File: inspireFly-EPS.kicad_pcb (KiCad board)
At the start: 4 copper layers, 88 x 94.5 mm, 2 parts

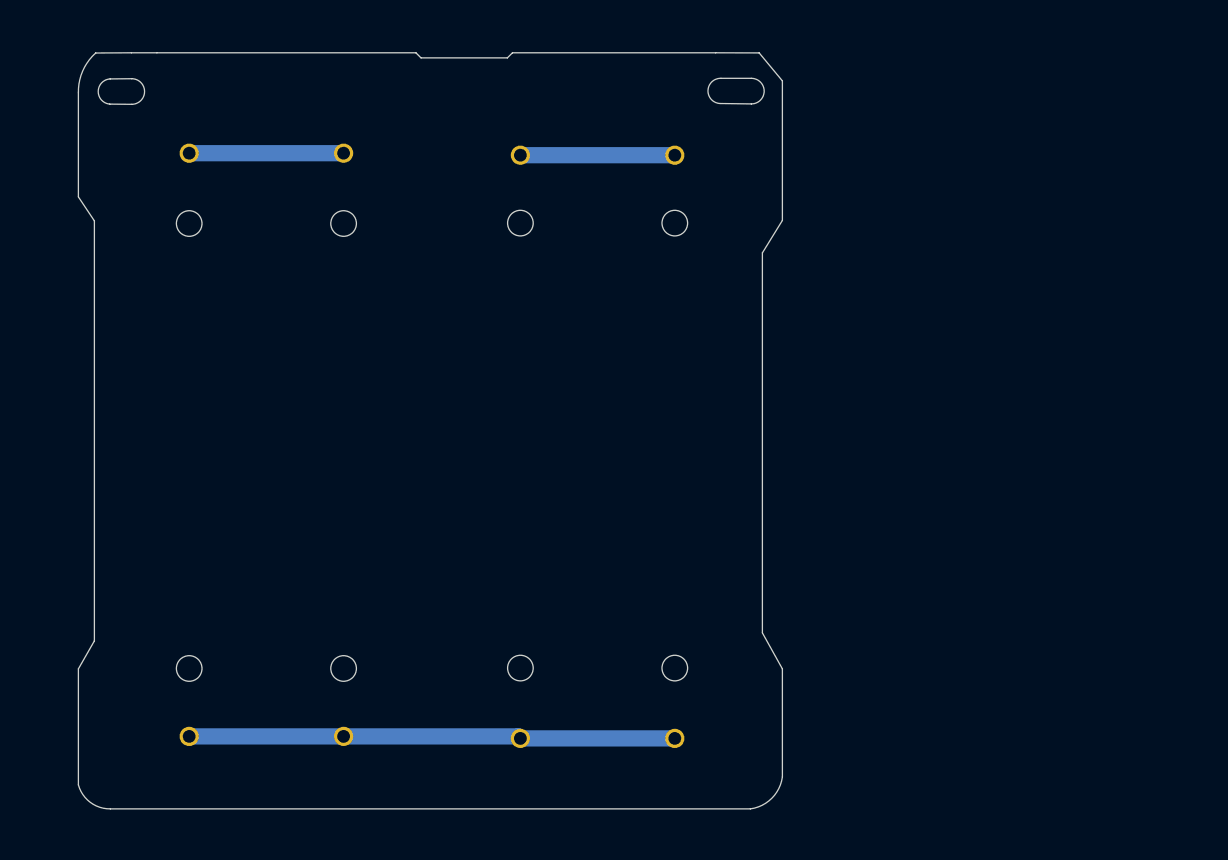
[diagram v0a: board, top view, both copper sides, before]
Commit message: Updates to BQ chip and routing
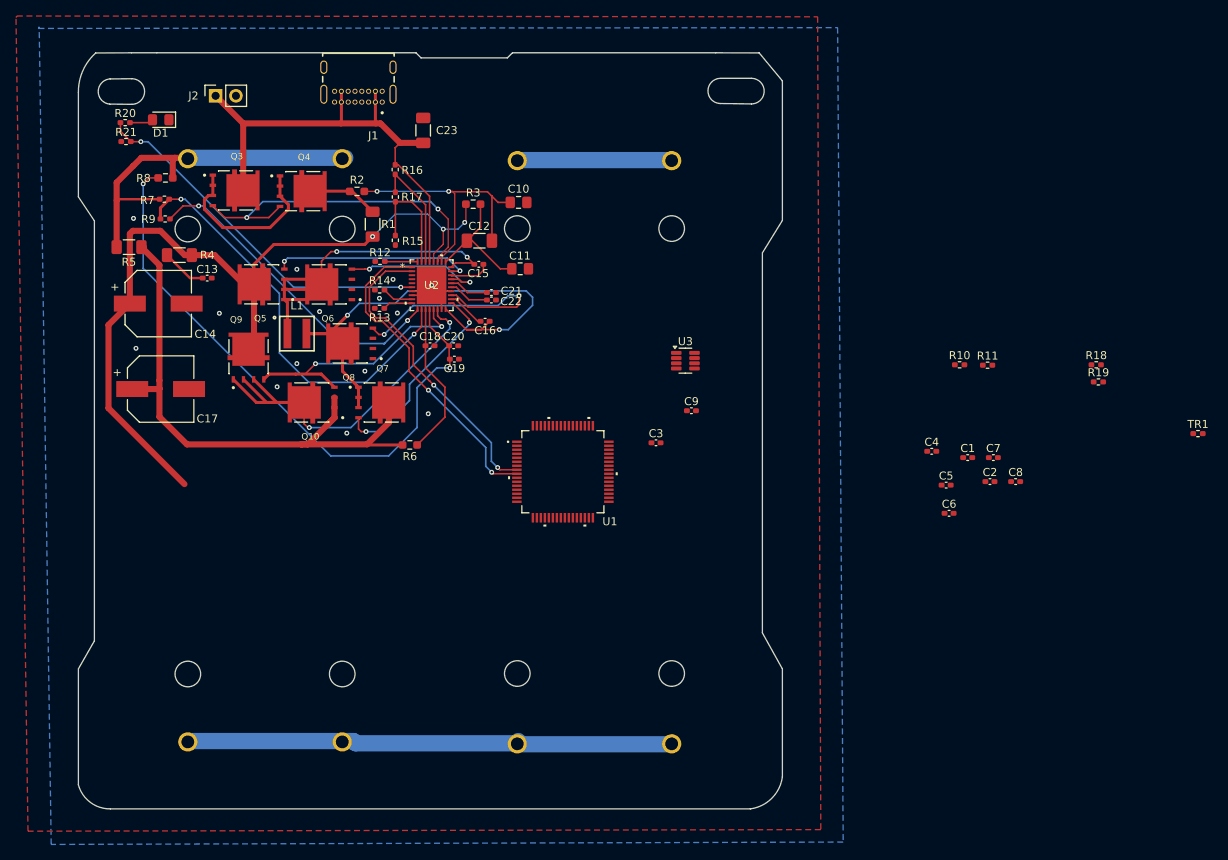
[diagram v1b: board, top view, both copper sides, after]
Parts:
- removed REF** (x2): BAT_BK-18650-PC4, inspireFly-EPS-footprints:BAT_BK-18650-PC4
- added BT1: BK-18650-PC4, inspireFly-EPS-footprints:BAT_BK-18650-PC4, B.Cu at (61.3, 74.8)
- added BT2: BK-18650-PC4, inspireFly-EPS-footprints:BAT_BK-18650-PC4, B.Cu at (102.5, 74.8)
- added C1: 100nF, Capacitor_SMD:C_0402_1005Metric_Pad0.74x0.62mm_HandSolder, F.Cu at (149.2, 75.6)
- added C10: 100nF, Capacitor_SMD:C_0805_2012Metric_Pad1.18x1.45mm_HandSolder, F.Cu at (93.0, 43.7)
- added C11: 100nF, Capacitor_SMD:C_0805_2012Metric_Pad1.18x1.45mm_HandSolder, F.Cu at (93.2, 52.0)
- added C12: 470nF, Capacitor_SMD:C_1206_3216Metric_Pad1.33x1.80mm_HandSolder, F.Cu at (88.1, 48.5)
- added C13: 2.2uF, Capacitor_SMD:C_0402_1005Metric_Pad0.74x0.62mm_HandSolder, F.Cu at (54.1, 53.2)
- added C14: 47uF, inspireFly-EPS-footprints:CAP_EEEFN1J470L, F.Cu at (48.0, 56.4)
- added C15: 47nF, Capacitor_SMD:C_0402_1005Metric_Pad0.74x0.62mm_HandSolder, F.Cu at (88.1, 51.4)
- added C16: 47nF, Capacitor_SMD:C_0402_1005Metric_Pad0.74x0.62mm_HandSolder, F.Cu at (88.8, 58.6)
- added C17: 47uF, inspireFly-EPS-footprints:CAP_EEEFN1J470L, F.Cu at (48.3, 67.0)
- added C18: 100nF, Capacitor_SMD:C_0402_1005Metric_Pad0.74x0.62mm_HandSolder, F.Cu at (82.0, 61.6)
- added C19: 100nF, Capacitor_SMD:C_0402_1005Metric_Pad0.74x0.62mm_HandSolder, F.Cu at (85.0, 63.3)
- added C2: 4.7uF, Capacitor_SMD:C_0402_1005Metric_Pad0.74x0.62mm_HandSolder, F.Cu at (151.9, 78.6)
- added C20: 470nF, Capacitor_SMD:C_0402_1005Metric_Pad0.74x0.62mm_HandSolder, F.Cu at (84.9, 61.6)
- added C21: 4.7uF, Capacitor_SMD:C_0402_1005Metric_Pad0.74x0.62mm_HandSolder, F.Cu at (89.6, 55.0)
- added C22: 4.7uF, Capacitor_SMD:C_0402_1005Metric_Pad0.74x0.62mm_HandSolder, F.Cu at (89.6, 55.9)
- added C23: 2.2uF, Capacitor_SMD:C_1206_3216Metric_Pad1.33x1.80mm_HandSolder, F.Cu at (81.1, 34.7)
- added C3: 100nF, Capacitor_SMD:C_0402_1005Metric_Pad0.74x0.62mm_HandSolder, F.Cu at (110.2, 73.8)
- added C4: 100nF, Capacitor_SMD:C_0402_1005Metric_Pad0.74x0.62mm_HandSolder, F.Cu at (144.7, 74.8)
- added C5: 100nF, Capacitor_SMD:C_0402_1005Metric_Pad0.74x0.62mm_HandSolder, F.Cu at (146.5, 79.0)
- added C6: 10uF, Capacitor_SMD:C_0402_1005Metric_Pad0.74x0.62mm_HandSolder, F.Cu at (146.8, 82.6)
- added C7: 1uF, Capacitor_SMD:C_0402_1005Metric_Pad0.74x0.62mm_HandSolder, F.Cu at (152.4, 75.6)
- added C8: 100nF, Capacitor_SMD:C_0402_1005Metric_Pad0.74x0.62mm_HandSolder, F.Cu at (155.2, 78.6)
- added C9: 100nF, Capacitor_SMD:C_0402_1005Metric_Pad0.74x0.62mm_HandSolder, F.Cu at (114.6, 69.7)
- added D1: LED, Diode_SMD:D_0805_2012Metric_Pad1.15x1.40mm_HandSolder, F.Cu at (48.3, 33.4)
- added J1: USB4085-GF-A_REVB, inspireFly-EPS-footprints:GCT_USB4085-GF-A_REVB, F.Cu at (73.0, 26.8)
- added J2: Conn_01x02_Pin, Connector_PinSocket_2.54mm:PinSocket_1x02_P2.54mm_Vertical, F.Cu at (55.1, 30.4)
- added L1: 2.2uH, inspireFly-EPS-footprints:WE-MXGI_4020, F.Cu at (65.3, 60.1)
- added Q10: SQJA62EP-T1_GE3, inspireFly-EPS-footprints:TRANS_SQJA62EP-T1_GE3, F.Cu at (67.3, 68.7)
- added Q3: SQJA62EP-T1_GE3, inspireFly-EPS-footprints:TRANS_SQJA62EP-T1_GE3, F.Cu at (57.5, 42.2)
- added Q4: SQJA62EP-T1_GE3, inspireFly-EPS-footprints:TRANS_SQJA62EP-T1_GE3, F.Cu at (65.9, 42.3)
- added Q5: SQJA62EP-T1_GE3, inspireFly-EPS-footprints:TRANS_SQJA62EP-T1_GE3, F.Cu at (61.0, 53.9)
- added Q6: SQJA62EP-T1_GE3, inspireFly-EPS-footprints:TRANS_SQJA62EP-T1_GE3, F.Cu at (69.5, 54.0)
- added Q7: SQJA62EP-T1_GE3, inspireFly-EPS-footprints:TRANS_SQJA62EP-T1_GE3, F.Cu at (75.7, 68.7)
- added Q8: SQJA62EP-T1_GE3, inspireFly-EPS-footprints:TRANS_SQJA62EP-T1_GE3, F.Cu at (72.1, 61.3)
- added Q9: SQJA62EP-T1_GE3, inspireFly-EPS-footprints:TRANS_SQJA62EP-T1_GE3, F.Cu at (59.3, 63.1)
- added R1: 5m, Resistor_SMD:R_1206_3216Metric_Pad1.30x1.75mm_HandSolder, F.Cu at (74.8, 46.4)
- added R10: 5.24k, Resistor_SMD:R_0402_1005Metric_Pad0.72x0.64mm_HandSolder, F.Cu at (148.2, 64.0)
- added R11: 30.31k, Resistor_SMD:R_0402_1005Metric_Pad0.72x0.64mm_HandSolder, F.Cu at (151.7, 64.0)
- added R12: 40k, Resistor_SMD:R_0402_1005Metric_Pad0.72x0.64mm_HandSolder, F.Cu at (75.7, 51.1)
- added R13: 3.3k, Resistor_SMD:R_0402_1005Metric_Pad0.72x0.64mm_HandSolder, F.Cu at (75.6, 56.9)
- added R14: 12.5k, Resistor_SMD:R_0402_1005Metric_Pad0.72x0.64mm_HandSolder, F.Cu at (75.7, 54.6)
- added R15: 22.6k, Resistor_SMD:R_0402_1005Metric_Pad0.72x0.64mm_HandSolder, F.Cu at (77.6, 48.4)
- added R16: 1M, Resistor_SMD:R_0402_1005Metric_Pad0.72x0.64mm_HandSolder, F.Cu at (77.6, 39.6)
- added R17: 100k, Resistor_SMD:R_0402_1005Metric_Pad0.72x0.64mm_HandSolder, F.Cu at (77.6, 43.0)
- added R18: 10k, Resistor_SMD:R_0402_1005Metric_Pad0.72x0.64mm_HandSolder, F.Cu at (165.2, 64.0)
- added R19: 10k, Resistor_SMD:R_0402_1005Metric_Pad0.72x0.64mm_HandSolder, F.Cu at (165.5, 66.1)
- added R2: 10, Resistor_SMD:R_0603_1608Metric_Pad0.98x0.95mm_HandSolder, F.Cu at (72.8, 42.3)
- added R20: 330, Resistor_SMD:R_0402_1005Metric_Pad0.72x0.64mm_HandSolder, F.Cu at (43.9, 33.7)
- added R21: 10K, Resistor_SMD:R_0402_1005Metric_Pad0.72x0.64mm_HandSolder, F.Cu at (44.0, 36.1)
- added R3: 10, Resistor_SMD:R_0603_1608Metric_Pad0.98x0.95mm_HandSolder, F.Cu at (87.3, 43.9)
- added R4: 2, Resistor_SMD:R_1206_3216Metric_Pad1.30x1.75mm_HandSolder, F.Cu at (50.6, 50.3)
- added R5: 5m, Resistor_SMD:R_1206_3216Metric_Pad1.30x1.75mm_HandSolder, F.Cu at (44.3, 49.3)
- added R6: 10, Resistor_SMD:R_0603_1608Metric_Pad0.98x0.95mm_HandSolder, F.Cu at (79.4, 74.0)
- added R7: 10, Resistor_SMD:R_0603_1608Metric_Pad0.98x0.95mm_HandSolder, F.Cu at (48.9, 40.6)
- added R8: 200k, Resistor_SMD:R_0402_1005Metric_Pad0.72x0.64mm_HandSolder, F.Cu at (48.8, 43.3)
- added R9: 44.8k, Resistor_SMD:R_0402_1005Metric_Pad0.72x0.64mm_HandSolder, F.Cu at (48.9, 45.8)
- added TR1: 120, Resistor_SMD:R_0402_1005Metric_Pad0.72x0.64mm_HandSolder, F.Cu at (177.9, 72.6)
- added U1: STM32U575RIT6, inspireFly-EPS-footprints:LQFP64-10x10mm_STM, F.Cu at (98.6, 77.4)
- added U2: BQ25750RRVR, inspireFly-EPS-footprints:VQFN36_RRV_TEX, F.Cu at (82.2, 54.1)
- added U3: TCAN332DCNR, Package_TO_SOT_SMD:SOT-23-8, F.Cu at (113.9, 63.5)
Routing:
- net V_PROTECTED: track 0.00 -> 102.8 mm, vias 0 -> 3
- net (no net): track 99.4 -> 0.00 mm
- net Net-(U2-SRP): track 0.00 -> 76.7 mm, vias 0 -> 2
- net Net-(Q10-S): track 0.00 -> 73.5 mm
- net Net-(Q7-S): track 0.00 -> 62.6 mm, vias 0 -> 2
- net USB_V: track 0.00 -> 62.1 mm
- net Net-(BT1-Pad1-): track 0.00 -> 60.4 mm
- net Net-(Q10-D): track 0.00 -> 56.0 mm, vias 0 -> 2
- net Net-(U2-FB): track 0.00 -> 53.4 mm, vias 0 -> 2
- net Net-(Q5-S): track 0.00 -> 48.5 mm, vias 0 -> 2
- net BAT +: track 0.00 -> 46.0 mm
- net POWER_GOOD: track 0.00 -> 45.6 mm, vias 0 -> 2
- net Net-(Q3-G): track 0.00 -> 42.5 mm, vias 0 -> 2
- net Net-(U2-FBG): track 0.00 -> 40.8 mm, vias 0 -> 2
- net I2C3-SDA: track 0.00 -> 40.4 mm, vias 0 -> 2
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- added copper zone on B.Cu, net BAT -
- added copper zone on F.Cu, net BAT -
- added copper zone on In1.Cu, net BAT -

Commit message: reroute of BQ chip
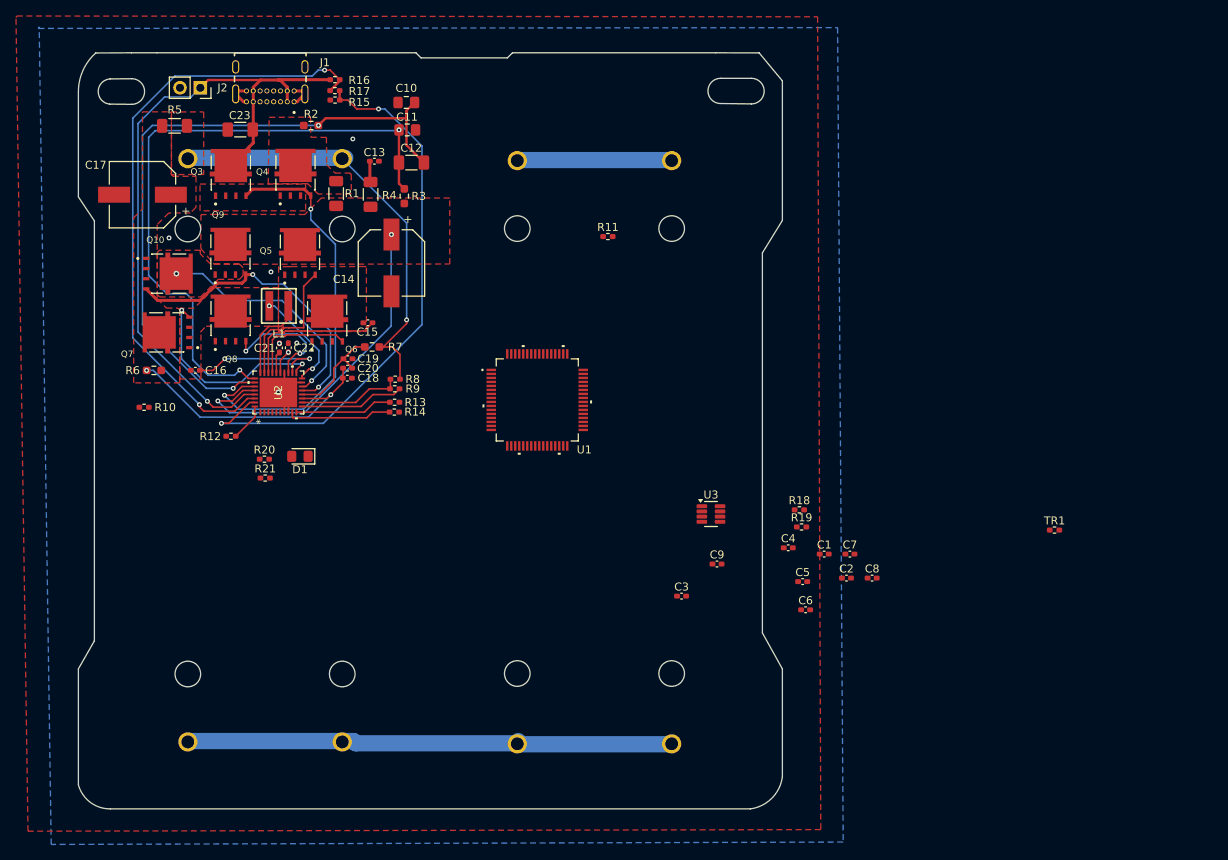
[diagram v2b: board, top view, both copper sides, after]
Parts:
- moved R10 102.1 mm to (46.2, 69.3), turned to 180 degrees
- moved R11 50.1 mm to (104.2, 48.0)
- moved D1 45.5 mm to (65.7, 75.4)
- moved R20 45.5 mm to (61.3, 75.8)
- moved R21 45.5 mm to (61.4, 78.2)
- moved R18 41.3 mm to (128.1, 82.1)
- moved R19 41.3 mm to (128.4, 84.3)
- moved C16 36.7 mm to (52.6, 64.7), turned to 180 degrees
- moved R8 36.6 mm to (77.6, 65.8), turned to 180 degrees
- moved R9 35.7 mm to (77.5, 67.0)
- moved R7 33.4 mm to (74.7, 61.8)
- moved R6 33.3 mm to (47.4, 64.7), turned to 0 degrees
- moved C14 29.6 mm to (77.1, 51.3), turned to -90 degrees
- moved R12 28.7 mm to (57.1, 72.9)
- moved Q7 28.0 mm to (49.2, 60.0), turned to 180 degrees
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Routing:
- net Net-(Q10-S): track 73.5 -> 0.00 mm
- net Net-(U2-ACN): track 16.1 -> 80.1 mm, vias 0 -> 2
- net Net-(U2-SRP): track 76.7 -> 13.2 mm, vias 2 -> 0
- net Net-(U2-ACUV): track 14.7 -> 78.1 mm, vias 0 -> 2
- net V_PROTECTED: track 102.8 -> 43.5 mm, vias 3 -> 2
- net Net-(U2-ACOV): track 14.3 -> 71.6 mm, vias 0 -> 2
- net Net-(U2-ACP): track 34.5 -> 85.0 mm
- net Net-(Q7-S): track 62.6 -> 13.1 mm
- net POWER_GOOD: track 45.6 -> 0.00 mm, vias 2 -> 0
- net Net-(U2-FB): track 53.4 -> 12.9 mm, vias 2 -> 0
- net I2C3-SDA: track 40.4 -> 0.00 mm, vias 2 -> 0
- net I2C3-SCL: track 38.5 -> 0.00 mm, vias 2 -> 0
- net Net-(Q5-S): track 48.5 -> 10.7 mm, vias 2 -> 0
- net Net-(U2-FBG): track 40.8 -> 13.1 mm, vias 2 -> 0
- net Net-(Q10-D): track 56.0 -> 29.2 mm
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- added copper zone on F.Cu, net BAT +
- added copper zone on F.Cu, net Net-(Q10-D)
- added copper zone on F.Cu, net Net-(Q10-S)
- added copper zone on F.Cu, net Net-(Q3-S)
- added copper zone on F.Cu, net Net-(Q4-D)
- added copper zone on F.Cu, net Net-(Q5-S)
- added copper zone on F.Cu, net Net-(Q7-S)
- added copper zone on F.Cu, net V_PROTECTED

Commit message: Placed STM chip
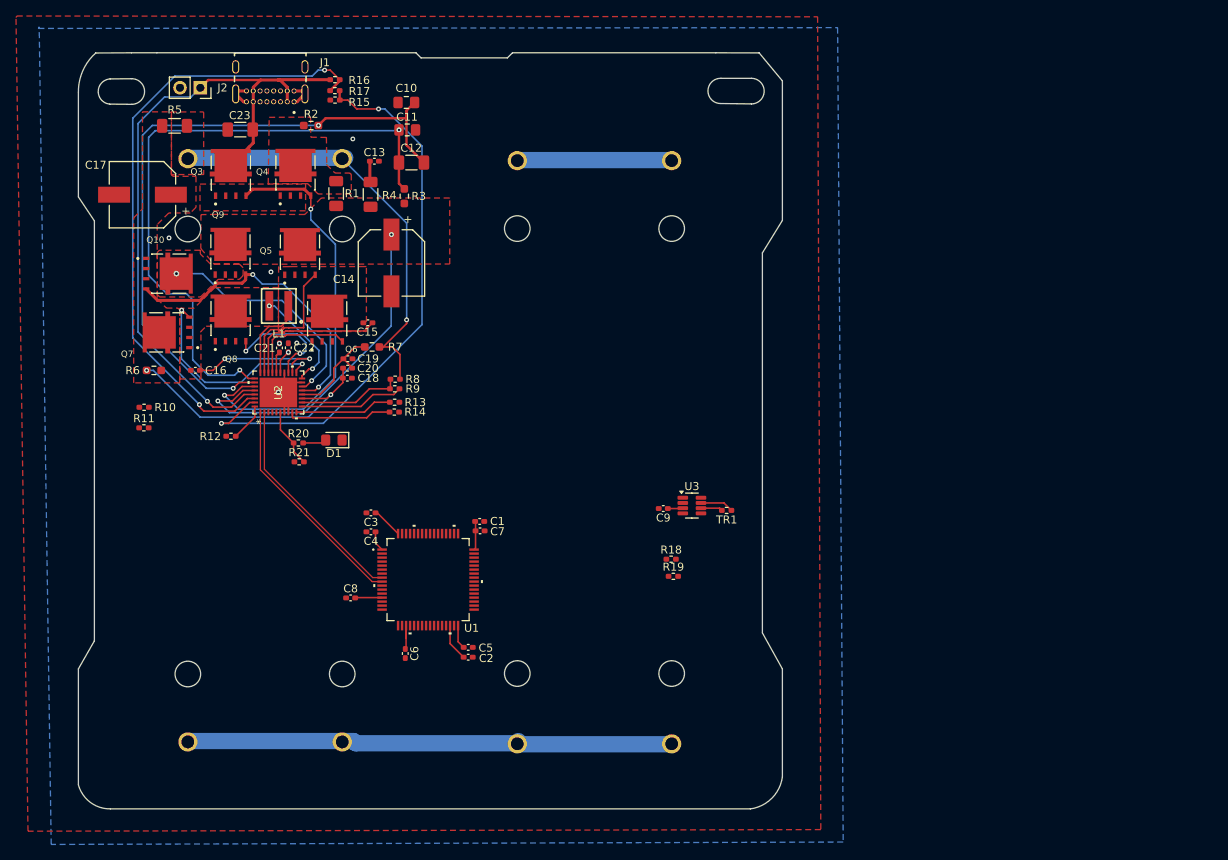
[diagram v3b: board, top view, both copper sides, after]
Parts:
- moved C8 65.2 mm to (72.0, 93.1), turned to 180 degrees
- moved R11 62.7 mm to (46.2, 71.9)
- moved C4 52.2 mm to (74.6, 84.9), turned to 180 degrees
- moved C6 50.3 mm to (78.9, 100.1), turned to -90 degrees
- moved C2 48.3 mm to (86.7, 100.6)
- moved C7 46.3 mm to (88.2, 84.8)
- moved C1 43.3 mm to (88.2, 83.6)
- moved C5 42.6 mm to (86.7, 99.3)
- moved TR1 41.1 mm to (119.0, 82.2), turned to 180 degrees
- moved C3 40.2 mm to (74.6, 82.5), turned to 180 degrees
- moved U1 26.3 mm to (81.7, 90.9)
- moved R18 17.2 mm to (112.1, 88.3)
- moved R19 17.2 mm to (112.4, 90.4)
- moved C9 9.66 mm to (111.1, 82.0), turned to 180 degrees
- moved D1 4.71 mm to (69.9, 73.4)
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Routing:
- net I2C3-SDA: track 0.00 -> 28.2 mm
- net I2C3-SCL: track 0.00 -> 27.5 mm
- net +3.3V: track 0.00 -> 23.0 mm
- net POWER_GOOD: track 0.00 -> 7.44 mm
- net Net-(U1B-VCAP): track 0.00 -> 4.65 mm
- net CAN_H: track 0.00 -> 4.19 mm
- net Net-(D1-A): track 0.00 -> 2.96 mm
- net CAN_L: track 0.00 -> 2.72 mm

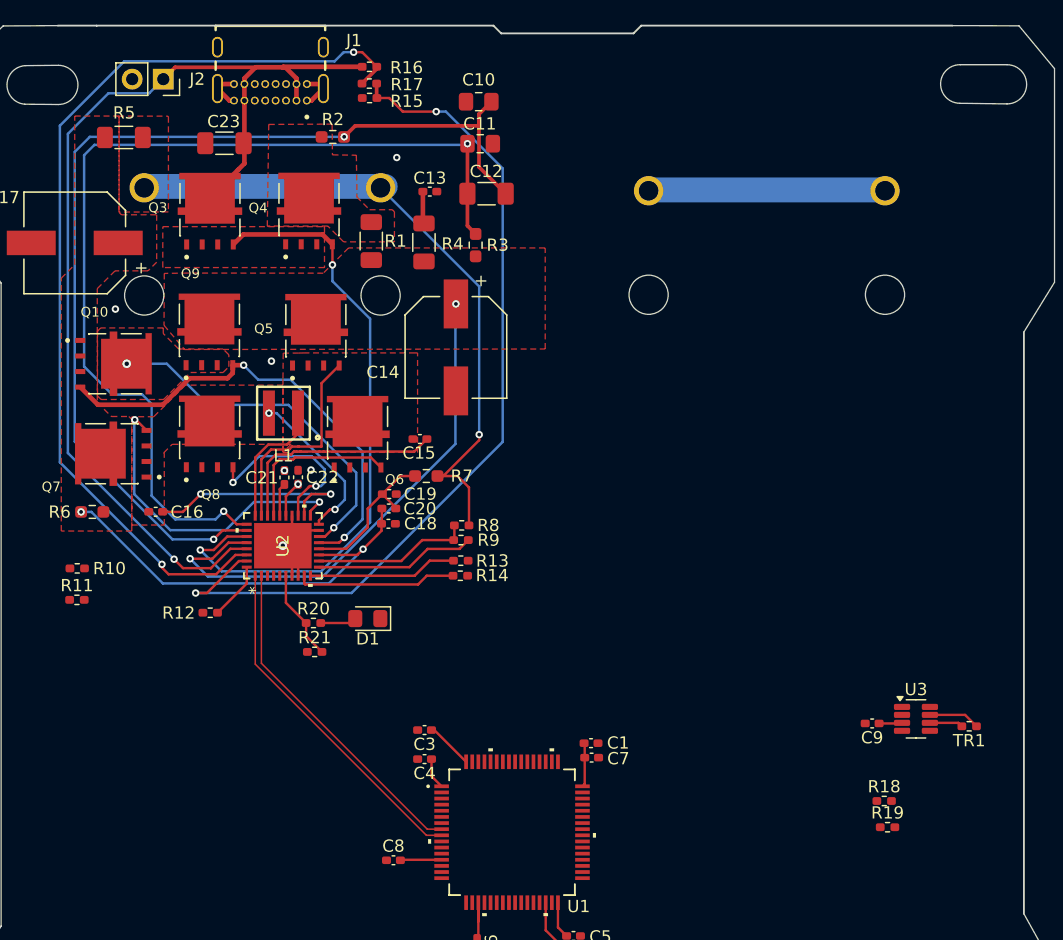
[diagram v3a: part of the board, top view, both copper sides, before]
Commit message: routed usb c
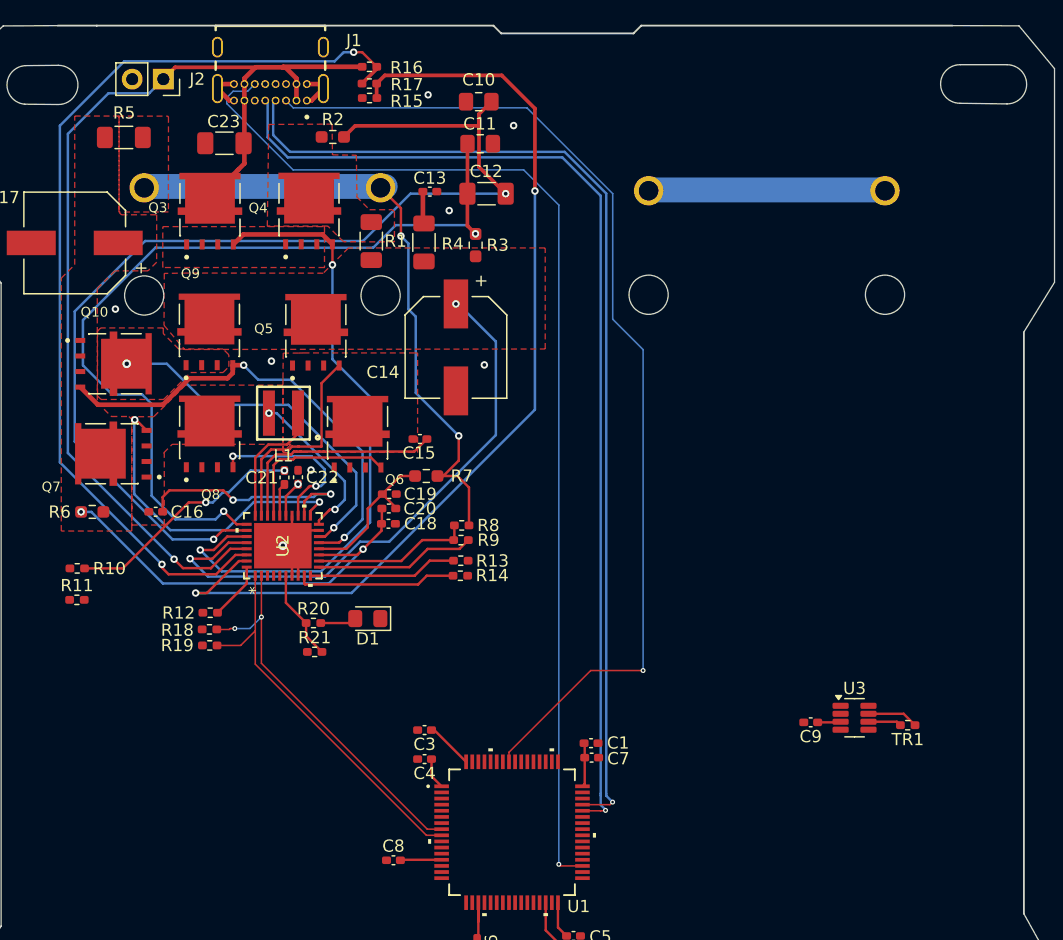
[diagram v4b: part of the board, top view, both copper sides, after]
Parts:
- moved R19 57.3 mm to (57.0, 75.6), turned to 180 degrees
- moved R18 56.8 mm to (57.0, 74.3), turned to 180 degrees
- moved C9 5.02 mm to (106.1, 81.9)
- moved TR1 5.02 mm to (114.0, 82.1)
- moved U3 5.02 mm to (109.7, 81.5)
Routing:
- net USB_CC2: track 0.00 -> 89.6 mm, vias 0 -> 1
- net USB_D+: track 0.00 -> 84.5 mm, vias 0 -> 1
- net USB_D-: track 0.00 -> 84.5 mm, vias 0 -> 1
- net USB_CC1: track 0.00 -> 84.3 mm, vias 0 -> 1
- net REGEN: track 0.00 -> 19.6 mm, vias 1 -> 2
- net Net-(U2-ACN): track 80.1 -> 70.6 mm
- net Net-(U2-ACOV): track 71.6 -> 79.2 mm
- net V_PROTECTED: track 43.5 -> 47.6 mm
- net I2C3-SCL: track 27.5 -> 31.5 mm, vias 0 -> 2
- net Net-(U2-ACP): track 85.0 -> 88.6 mm
- net I2C3-SDA: track 28.2 -> 31.8 mm
- net BAT +: track 54.1 -> 52.7 mm, vias 1 -> 2
- net Net-(U2-BTST2): track 17.9 -> 19.3 mm
- net Net-(Q8-G): track 15.3 -> 14.1 mm
- net BAT -: vias 5 -> 8
